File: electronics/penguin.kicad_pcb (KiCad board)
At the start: 4 copper layers, 89.5 x 62.6 mm, 146 parts, among them IC1 HY2120-AB, J1 USB_C_CONN, J10 MTR_HEADER_2, J2 CAM_HEADER, J3 BATT_BALANCE_HEADER, J4 TOF_HEADER, J6 IR_HEADER_1, J7 IR_HEADER_2, J8 BATT_CONN, J9 MTR_HEADER_1, Q1 AO3400A, Q2 SI2393DS, Q3 2N7002, Q4 FS8205A, SW1 SW_Boot, SW2 SW_Reset, U1 ESP32-S3-WROOM-1U-N8R8, U2 LP5907MFX-2.8, U3 LP5907MFX-1.2, U4 DRV8833PW, U5 MCP23017_ML, U6 TPS5405DR, U7 AMS1117-3.3, U8 DMP4065S-7

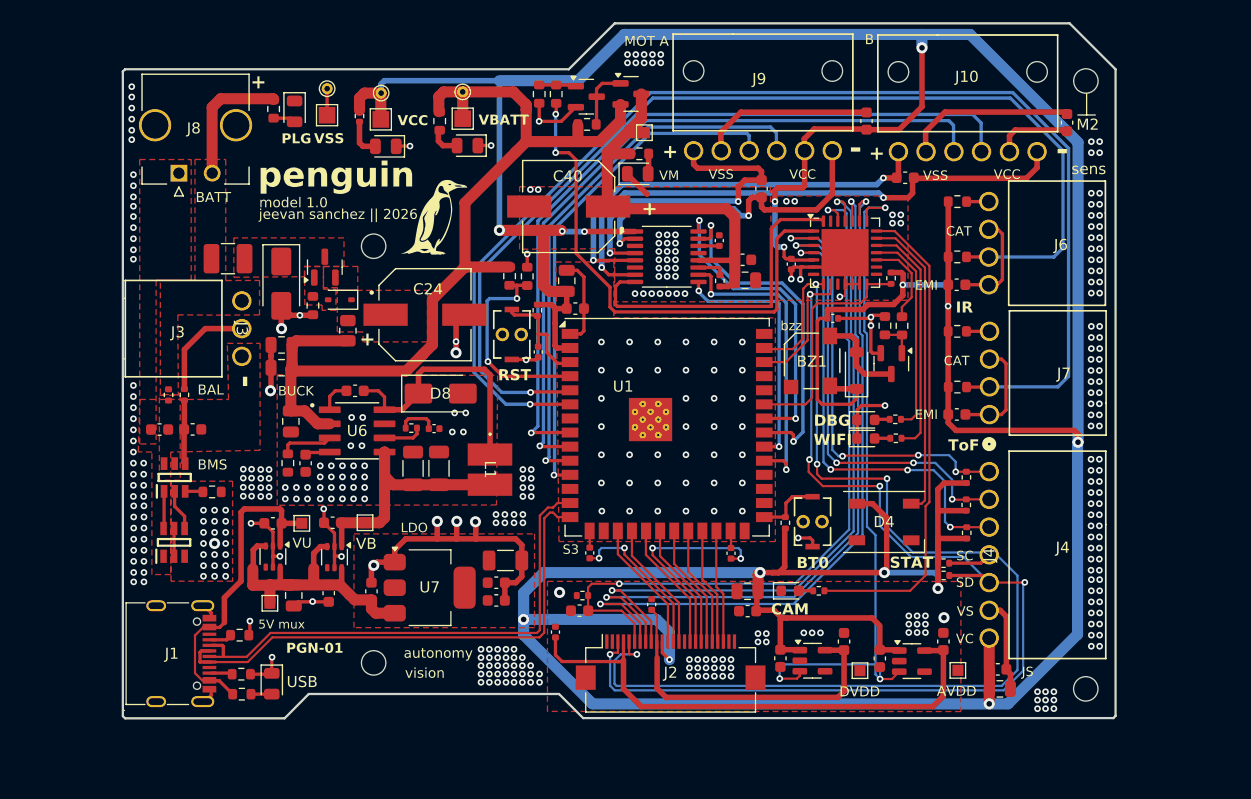
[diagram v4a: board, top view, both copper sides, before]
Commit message: add IMU and redo BMS pours
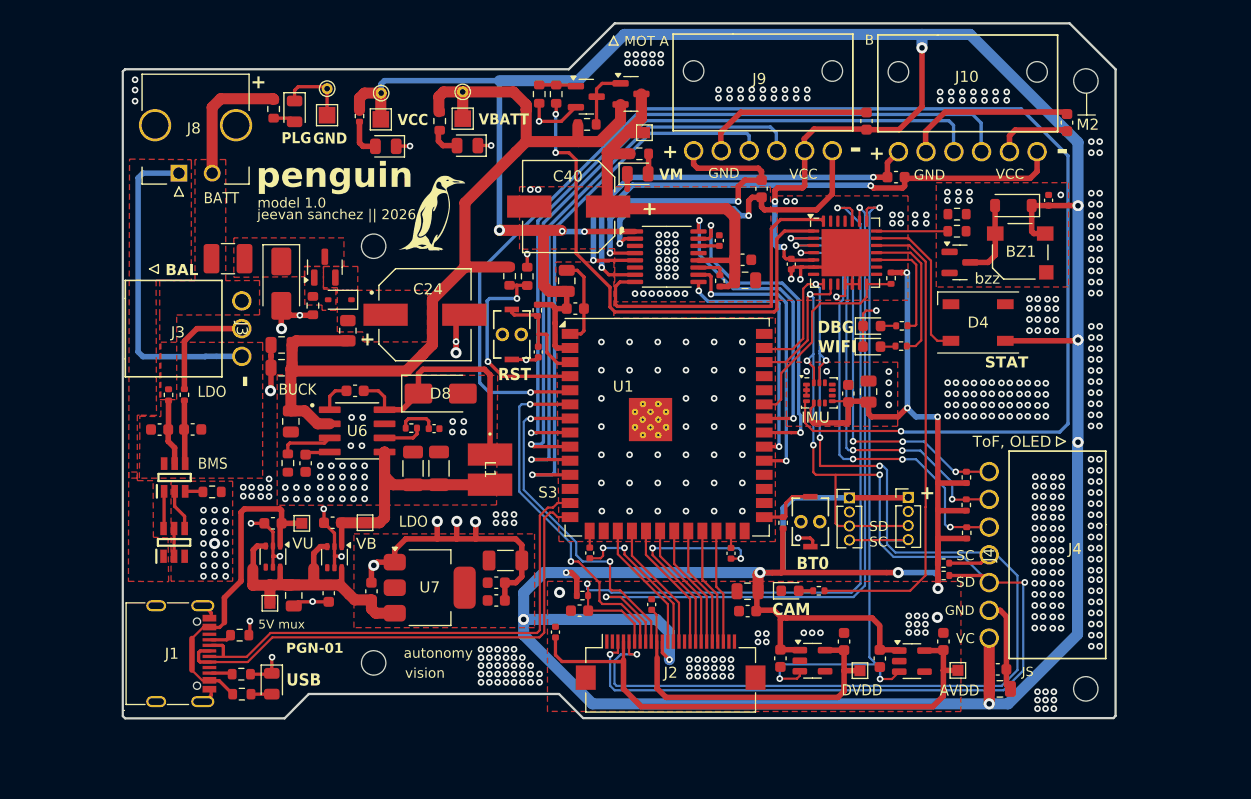
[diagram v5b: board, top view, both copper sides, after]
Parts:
- removed C47: 0.1uF, Capacitor_SMD:C_0603_1608Metric
- removed J7: IR_HEADER_2, MOLEX_NANO_4:CONN_SD-105313-100_04_MOL
- removed R30, R31: 200, Resistor_SMD:R_0603_1608Metric
- removed R32, R33: 10k, Resistor_SMD:R_0603_1608Metric
- added ?: , clipboard:fc8df92e-a3b3-4f73-a46e-2aabbf2af471, F.Cu at (139.5, 60.4)
- added ?: , clipboard:fc8df92e-a3b3-4f73-a46e-2aabbf2af471, F.Cu at (179.8, 95.7)
- added ?: , clipboard:fc8df92e-a3b3-4f73-a46e-2aabbf2af471, F.Cu at (98.9, 81.0)
- added C13: 10uF, Capacitor_SMD:C_0805_2012Metric, F.Cu at (162.9, 91.7)
- added J5: I2C_JUMPER, Connector_PinHeader_1.27mm:PinHeader_1x04_P1.27mm_Vertical, F.Cu at (161.2, 101.2)
- added NT1: GND, NetTie:NetTie-2_SMD_Pad0.5mm, B.Cu at (103.6, 88.5)
- added U9: LSM6DSL, Package_LGA:LGA-14_3x2.5mm_P0.5mm_LayoutBorder3x4y, F.Cu at (158.4, 91.8)
- J6: value IR_HEADER_1 -> I2C_JUMPER; footprint MOLEX_NANO_4:CONN_SD-105313-100_04_MOL -> Connector_PinHeader_1.27mm:PinHeader_1x04_P1.27mm_Vertical
- moved J6 27.6 mm to (166.4, 101.2), turned to 0 degrees
- moved C15 22.2 mm to (179.1, 74.4), turned to 90 degrees
- moved BZ1 21.2 mm to (176.5, 79.0), turned to 180 degrees
- moved D13 20.5 mm to (175.9, 74.9), turned to 180 degrees
- moved D4 19.9 mm to (172.8, 85.4), turned to 180 degrees
- moved R12 12.0 mm to (170.8, 75.7), turned to 0 degrees
- moved Q1 11.0 mm to (171.1, 80.0), turned to 0 degrees
- moved R10 10.1 mm to (165.9, 85.7)
- moved D3 10.1 mm to (163.2, 85.7)
- moved C46 9.96 mm to (161.1, 91.8), turned to -90 degrees
- moved R11 9.86 mm to (170.8, 77.2), turned to 180 degrees
- moved D2 6.62 mm to (163.2, 87.6)
- moved R9 6.62 mm to (165.8, 87.5)
- moved C18 0.83 mm to (165.3, 72.3)
- moved G*** 0.42 mm to (123.5, 75.6)
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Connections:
- net CAM_EN renamed CAM_PEN
- C44 pad 1: BATT_N -> VSS_SENSE
- C45 pad 1: BATT_N -> VSS_SENSE
- C46 pad 1: +3V3 -> GND
- C46 pad 2: GND -> +3V3
- IC1 pad 6: BATT_N -> VSS_SENSE
- J3 pad 1: BATT_N -> VSS_SENSE
- J6 pad 1: Net-(J6-Pin_1) -> +3V3
- J6 pad 3: IR_DATA_1 -> SDA
- J6 pad 4: GND -> SCL
- R10 pad 1: WIFI_LED -> DBG_LED
- R9 pad 1: DBG_LED -> WIFI_LED
- U1 pad 5: IR_DATA_1 -> IMU_INT
- U1 pad 6: IR_DATA_2 -> CAM_VSYNC
- U1 pad 7: unconnected-(U1-IO7-Pad7) -> CAM_HREF
- U5 pad 17: BUZZ_EN -> DBG_LED
- U5 pad 18: DBG_LED -> WIFI_LED
- U5 pad 19: WIFI_LED -> CAM_STATUS
- U5 pad 21: CAM_STATUS -> BUZZ_EN
- U5 pad 23: CAM_VSYNC -> CAM_PWDN_EN
- U5 pad 24: CAM_PWDN_EN -> CAM_RST
- U5 pad 25: CAM_HREF -> unconnected-(U5-GPB0-Pad25)
- U5 pad 26: CAM_RST -> unconnected-(U5-GPB1-Pad26)
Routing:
- net IMU_INT: track 0.00 -> 130.0 mm, vias 0 -> 2
- net IR_DATA_2: track 111.6 -> 0.00 mm, vias 1 -> 0
- net IR_DATA_1: track 96.8 -> 0.00 mm, vias 1 -> 0
- net CAM_VSYNC: track 64.8 -> 31.7 mm
- net CAM_HREF: track 63.4 -> 30.8 mm
- net BATT_N: track 0.00 -> 25.8 mm
- net GND: track 179.5 -> 155.7 mm, vias 401 -> 512
- net SDA: track 107.9 -> 123.1 mm, vias 5 -> 6
- net RGB_DATA: track 27.8 -> 14.4 mm
- net SCL: track 108.1 -> 119.4 mm, vias 4 -> 5
- net DBG_LED: track 18.7 -> 10.00 mm
- net WIFI_LED: track 21.5 -> 12.9 mm
- net Net-(IC1-VDD): track 0.00 -> 5.93 mm
- net CAM_RST: track 66.2 -> 71.8 mm
- net ENC_A_PH2: track 47.0 -> 50.8 mm
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- added copper zone on F.Cu, net VSS_SENSE
- removed copper zone on F.Cu, net Net-(IC1-VDD)
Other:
- board text added: "GND"
- board text added: "IMU"
- board text added: "ToF, OLED"
- board text added: "jeevansanchez.com"
- board text added: "may 2026"
- board text removed: "CAT"
- board text removed: "EMI"
- board text removed: "IR"
- board text removed: "IR-1"
- board text removed: "IR-2"
- board text removed: "TOF-1"
- board text removed: "ToF"
- board text removed: "VS"
- board text removed: "VSS"
- board text removed: "sens"
